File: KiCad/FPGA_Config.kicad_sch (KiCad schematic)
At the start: 8 parts, among them SW501 SW_Omron_B3FS, U502 XC7S50FTGB196

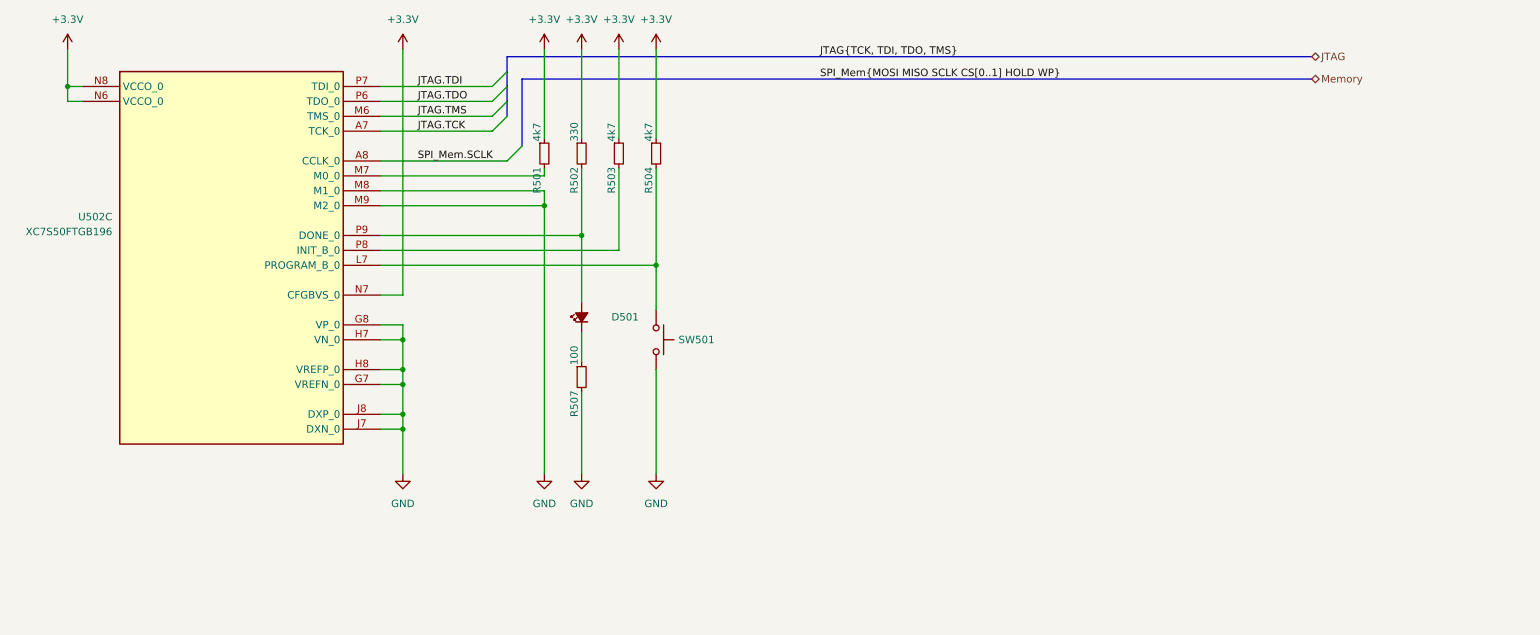
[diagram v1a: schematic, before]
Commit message: LEDs zur Visualisierung des ausgewählten FPGAs
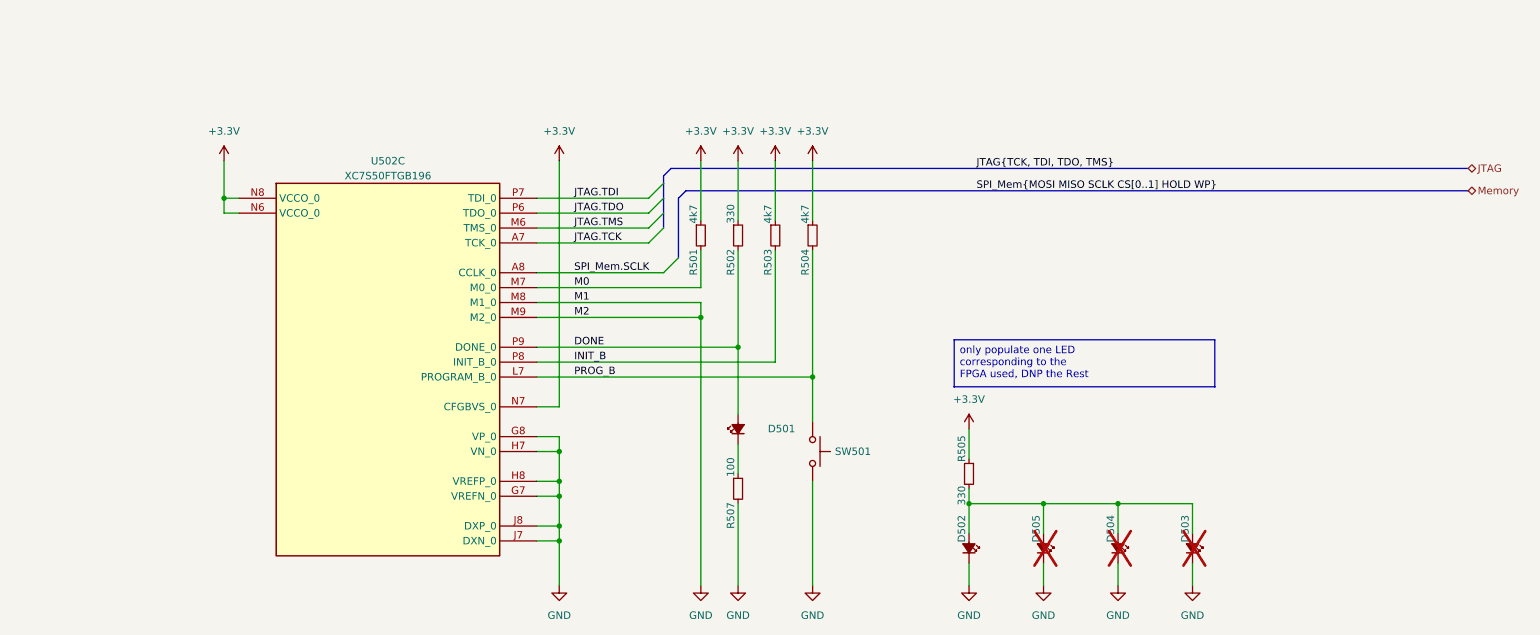
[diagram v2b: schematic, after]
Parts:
- added D502, D503, D504, D505: LED_Small_Filled, Library:LED_0603_1608Metric_Box, symbol Device:LED_Small_Filled
- added R505: 330, Resistor_SMD:R_0402_1005Metric, symbol Device:R_Small
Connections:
- net +3.3V: now also R505.1
- net GND: now also D502.1 (K), D503.1 (K), D504.1 (K), D505.1 (K)
- net PROG_B: now reaches R504.2, SW501.1, U502.L7 (PROGRAM_B_0)
- net M0: now reaches R501.2, U502.M7 (M0_0)
- net INIT_B: now reaches R503.2, U502.P8 (INIT_B_0)
- net DONE: now reaches D501.2 (A), R502.2, U502.P9 (DONE_0)
- new net: D502.2 (A), D503.2 (A), D504.2 (A), D505.2 (A), R505.2
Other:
- moved on the sheet: D501, R501, R502, R503, R504, R507, SW501, U502C

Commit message: JTAG-Verbinder hinzugefügt
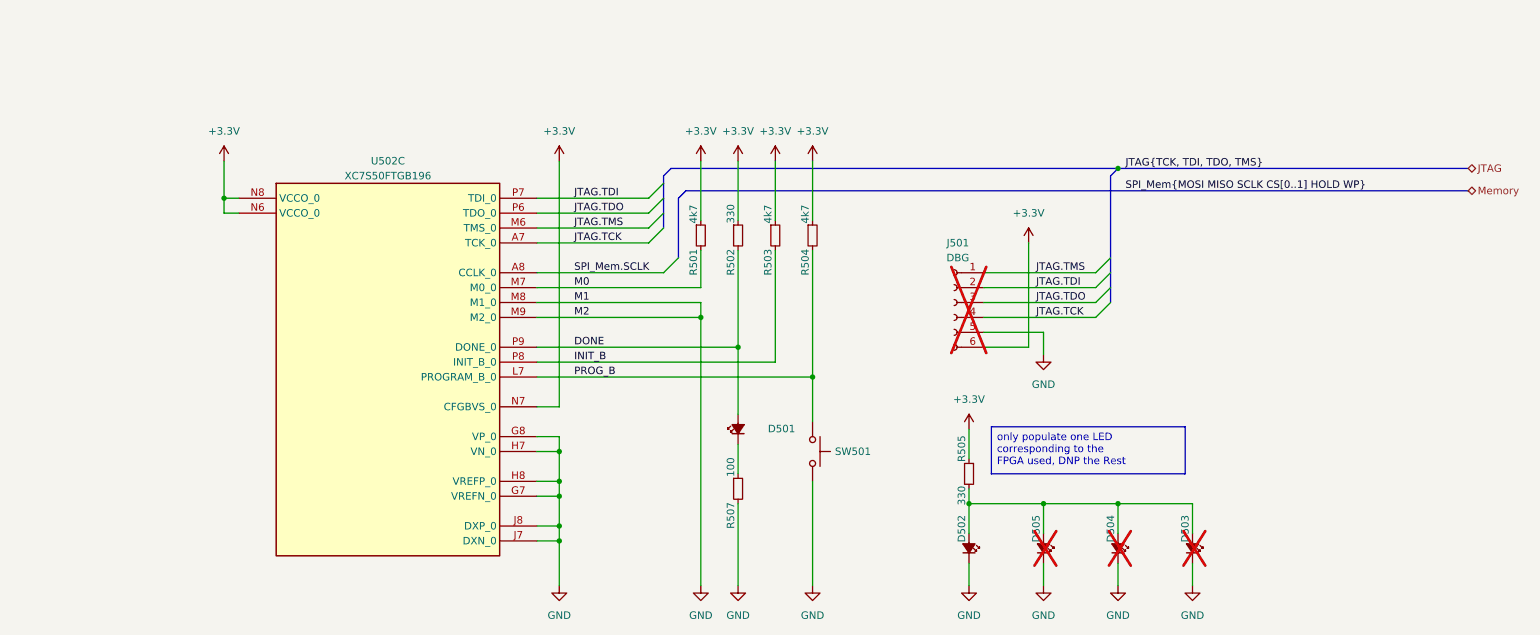
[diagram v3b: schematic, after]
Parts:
- added J501: DBG, Library:PinHeader_1x06_P2.54mm_Vertical_versetzt, symbol Connector:Conn_01x06_Socket
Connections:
- net +3.3V: now also J501.6 (Pin_6)
- net GND: now also J501.5 (Pin_5)
- net JTAG.TCK: now also J501.4 (Pin_4)
- net JTAG.TDI: now also J501.2 (Pin_2)
- net JTAG.TDO: now also J501.3 (Pin_3)
- net JTAG.TMS: now also J501.1 (Pin_1)
